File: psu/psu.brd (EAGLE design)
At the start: 31 x 67 mm, 8 parts

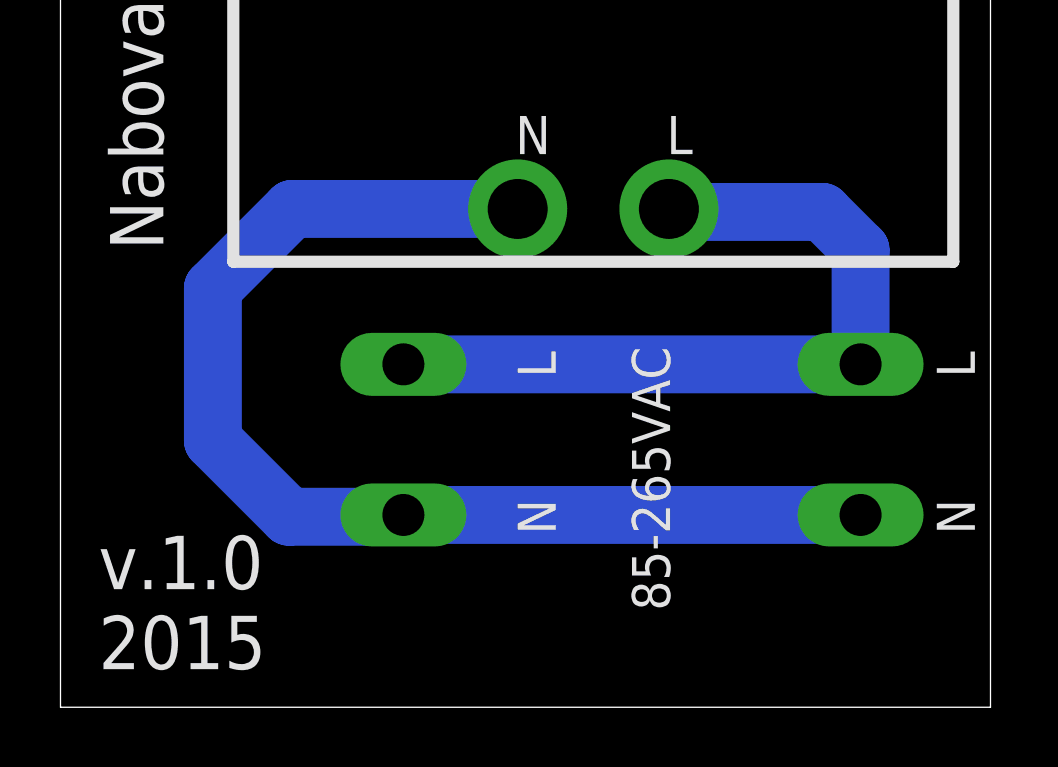
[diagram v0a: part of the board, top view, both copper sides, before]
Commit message: psu: ac connectors moved
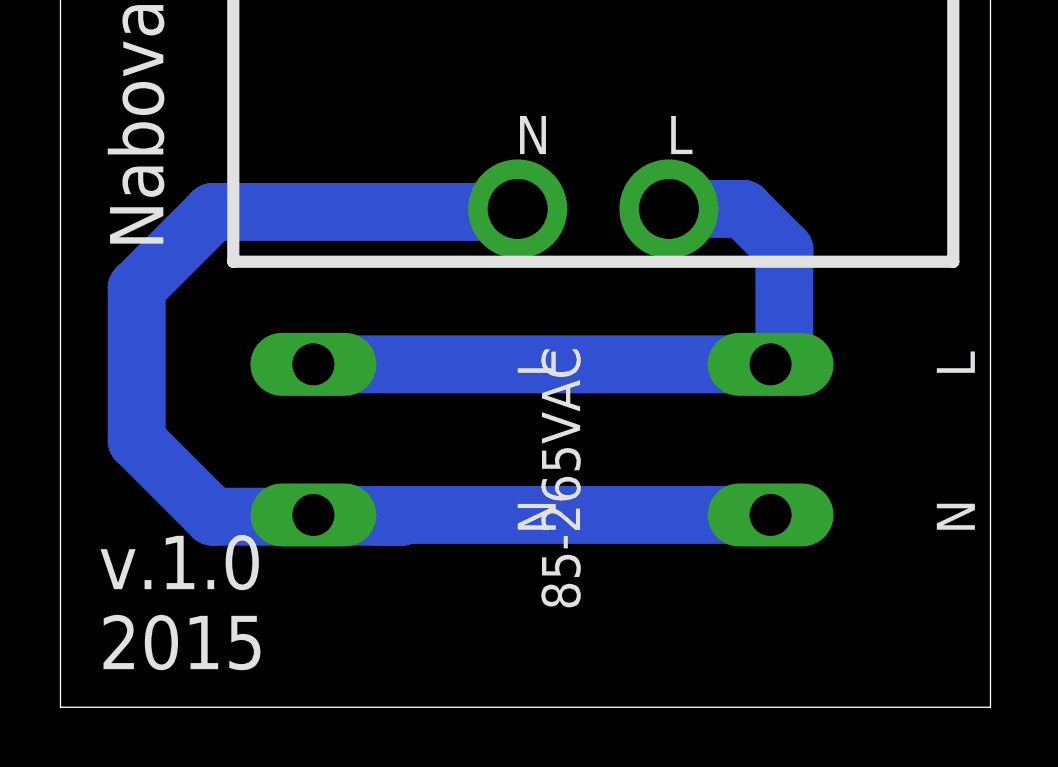
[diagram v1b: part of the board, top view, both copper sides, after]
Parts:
- moved 85-265VAC 3.00 mm to (23.7, 11.4)
- moved 85-265VAC1 3.00 mm to (8.43, 11.4)
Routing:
- net N$2: track 39.0 -> 46.9 mm
- net N$1: track 26.0 -> 23.7 mm
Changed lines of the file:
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@@
 <setting verticaltext="up"/>
 </settings>
-<grid distance="0.05" unitdist="inch" unit="mil" style="dots" multiple="1" display="no" altdistance="0.025" altunitdist="inch" altunit="inch"/>
+<grid distance="0.05" unitdist="inch" unit="inch" style="dots" multiple="1" display="no" altdistance="0.025" altunitdist="inch" altunit="inch"/>
 <layers>
 <layer number="1" name="Top" color="4" fill="1" visible="yes" active="yes"/>
@@
 <attribute name="NAME" x="21.4538" y="60.8588" size="1.27" layer="25"/>
 </element>
-<element name="85-265VAC" library="SparkFun (old)" package="1X02_LONGPADS" value="" x="26.67" y="11.43" smashed="yes" rot="R270">
-<attribute name="NAME" x="19.05" y="7.62" size="1.27" layer="25" rot="R270" align="bottom-center"/>
+<element name="85-265VAC" library="SparkFun (old)" package="1X02_LONGPADS" value="" x="23.67" y="11.43" smashed="yes" rot="R270">
+<attribute name="NAME" x="16.05" y="7.62" size="1.27" layer="25" rot="R270" align="bottom-center"/>
 </element>
 <element name="JP2" library="SparkFun (old)" package="1X02_LONGPADS" value="" x="2.54" y="57.15" smashed="yes" rot="R270"/>
 <element name="U$1" library="SparkFun-Aesthetics" package="OSHW-LOGO-M" value="" x="2.54" y="63.5" rot="R90"/>
-<element name="85-265VAC1" library="SparkFun (old)" package="1X02_LONGPADS" value="" x="11.43" y="11.43" smashed="yes" rot="R270"/>
+<element name="85-265VAC1" library="SparkFun (old)" package="1X02_LONGPADS" value="" x="8.43" y="11.43" smashed="yes" rot="R270"/>
 </elements>
 <signals>
@@
 <contactref element="L" pad="1"/>
 <contactref element="85-265VAC1" pad="1"/>
-<wire x1="11.43" y1="11.43" x2="26.67" y2="11.43" width="1.9304" layer="16"/>
-<wire x1="26.67" y1="11.43" x2="26.67" y2="15.24" width="1.9304" layer="16"/>
-<wire x1="26.67" y1="15.24" x2="25.4" y2="16.51" width="1.9304" layer="16"/>
-<wire x1="25.4" y1="16.51" x2="20.38" y2="16.51" width="1.9304" layer="16"/>
-<wire x1="20.38" y1="16.51" x2="20.28" y2="16.61" width="1.9304" layer="16"/>
+<wire x1="8.43" y1="11.43" x2="23.67" y2="11.43" width="1.9304" layer="16"/>
+<wire x1="20.28" y1="16.61" x2="22.76" y2="16.61" width="1.9304" layer="16"/>
+<wire x1="22.76" y1="16.61" x2="24.13" y2="15.24" width="1.9304" layer="16"/>
+<wire x1="24.13" y1="15.24" x2="24.13" y2="11.89" width="1.9304" layer="16"/>
+<wire x1="24.13" y1="11.89" x2="23.67" y2="11.43" width="1.9304" layer="16"/>
 </signal>
 <signal name="N$2">
@@
 <contactref element="N" pad="1"/>
 <contactref element="85-265VAC1" pad="2"/>
-<wire x1="15.24" y1="16.61" x2="7.72" y2="16.61" width="1.9304" layer="16"/>
-<wire x1="7.72" y1="16.61" x2="5.08" y2="13.97" width="1.9304" layer="16"/>
-<wire x1="5.08" y1="13.97" x2="5.08" y2="8.89" width="1.9304" layer="16"/>
-<wire x1="5.08" y1="8.89" x2="7.62" y2="6.35" width="1.9304" layer="16"/>
-<wire x1="7.62" y1="6.35" x2="11.37" y2="6.35" width="1.9304" layer="16"/>
-<wire x1="11.37" y1="6.35" x2="11.43" y2="6.41" width="1.9304" layer="16"/>
-<wire x1="11.43" y1="6.41" x2="26.67" y2="6.41" width="1.9304" layer="16"/>
+<wire x1="5.08" y1="6.35" x2="11.37" y2="6.35" width="1.9304" layer="16"/>
+<wire x1="11.37" y1="6.35" x2="8.43" y2="6.41" width="1.9304" layer="16"/>
+<wire x1="8.43" y1="6.41" x2="23.67" y2="6.41" width="1.9304" layer="16"/>
+<wire x1="5.08" y1="6.35" x2="2.54" y2="8.89" width="1.9304" layer="16"/>
+<wire x1="2.54" y1="8.89" x2="2.54" y2="13.97" width="1.9304" layer="16"/>
+<wire x1="2.54" y1="13.97" x2="5.08" y2="16.51" width="1.9304" layer="16"/>
+<wire x1="5.08" y1="16.51" x2="15.14" y2="16.51" width="1.9304" layer="16"/>
+<wire x1="15.14" y1="16.51" x2="15.24" y2="16.61" width="1.9304" layer="16"/>
 </signal>
 <signal name="N$3">
